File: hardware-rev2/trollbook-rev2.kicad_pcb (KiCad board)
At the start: 4 copper layers, 100 x 100 mm, 150 parts, among them CON1 FPGA JTAG, CON2 CPU JTAG, P1 /BR, P2 /CDIS, P3 Audio, P4 ER-CON40HT-1, P5 Power, P6 Peripheral, P7 VGA, P8 Clocks, P9 Ext. Interrupt, Q1 2N7002E, Q2 2N7002E, Q3 DMP3030SN-7, Q4 2N7002E, Q5 2N7002E, U1 MC68040FC33V, U10 ADA4851-4, U11 33 MHz, U12 12.288 MHz, U2 EPF10K50VRC240, U3 EPC2, U4 HY57V561620, U5 HY57V561620, U6 AS7C34098, U7 74LVC138, U8 MCP4902, U9 S25FL204K0TMFI010

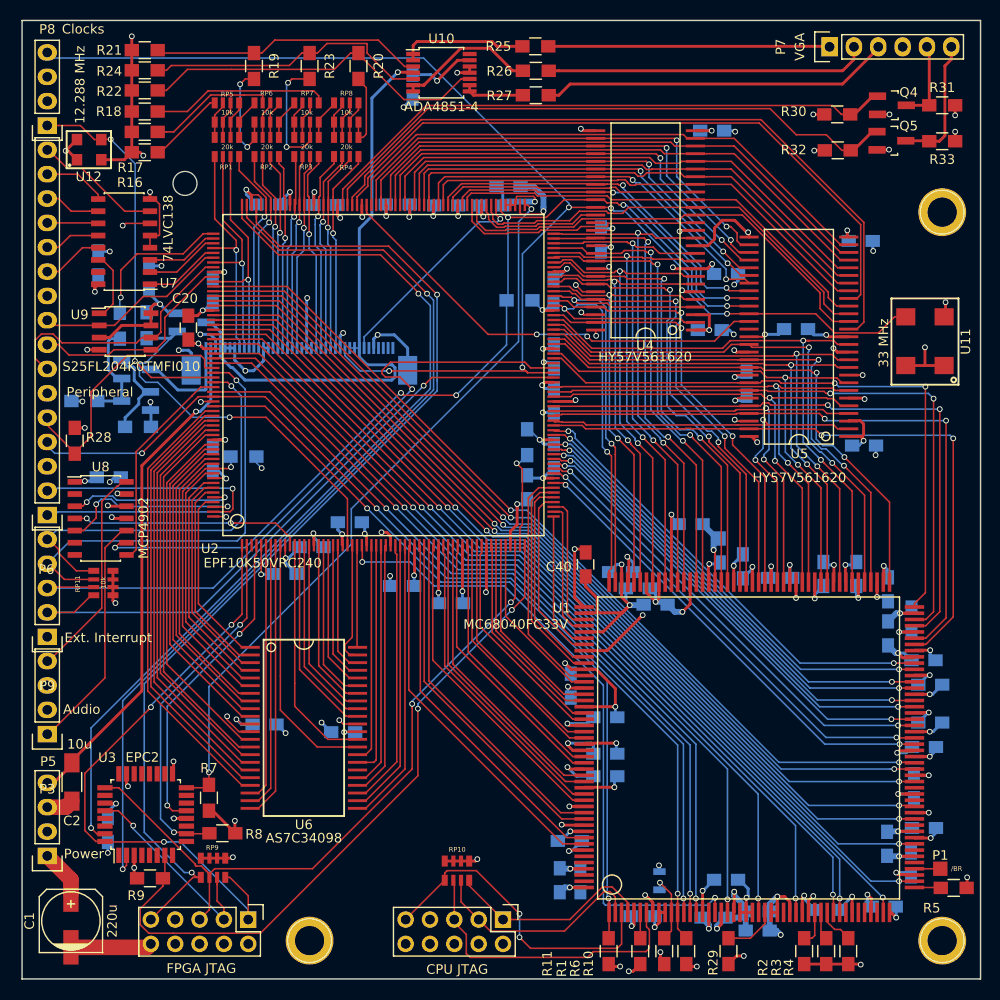
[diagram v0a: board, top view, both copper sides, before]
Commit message: added pcb logo
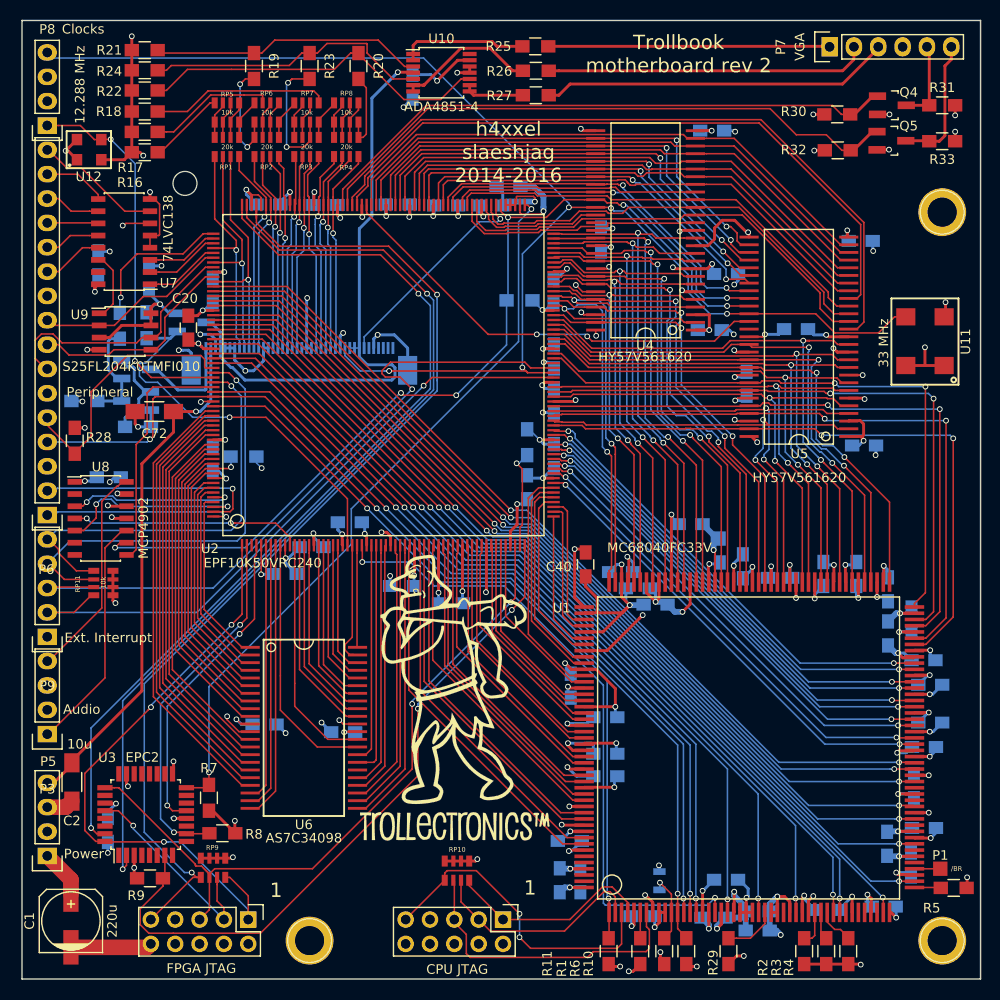
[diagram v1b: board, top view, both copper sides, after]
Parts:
- added C72: 1u, Capacitors_SMD:C_1206_HandSoldering, F.Cu at (98.8, 90.8)
- added G***: LOGO, mod:trollectronics-logo, F.Cu at (130.0, 120.8)
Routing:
- net /SNDSYNC: track 22.3 -> 25.2 mm
- net GND: track 413.5 -> 415.3 mm
- net /VGALED_ANODE: track 53.1 -> 54.5 mm
- net /CPURSTI: track 104.5 -> 105.6 mm
- net /LLA2: track 21.3 -> 20.6 mm
- net /LLD0: track 29.6 -> 29.0 mm
- net /LLD5: track 39.6 -> 38.9 mm
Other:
- board text added: "1"
- board text added: "Trollbook motherboard rev 2"
- board text added: "h4xxel slaeshjag 2014-2016"

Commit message: corrected solder mask minimum width, now there is solder stop everywhere
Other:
- rule solder_mask_min_width: 0.1016 -> 0.0762
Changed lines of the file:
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@@
 (kicad_pcb (version 4) (host pcbnew 0.201602281447+6595~42~ubuntu14.04.1-product)
   (general
-    (links 0)
+    (links 816)
     (no_connects 0)
-    (area 84.924999 49.924999 185.075001 150.075001)
+    (area 52.000001 38.468802 224.934721 153.800001)
     (thickness 1.6)
     (drawings 10)
@@
     (pad_drill 3.048)
     (pad_to_mask_clearance 0.0508)
-    (solder_mask_min_width 0.1016)
+    (solder_mask_min_width 0.0762)
     (aux_axis_origin 0 0)
     (visible_elements FFFFEF7F)
     (pcbplotparams
-      (layerselection 0x01030_ffffffff)
-      (usegerberextensions false)
+      (layerselection 0x010f0_ffffffff)
+      (usegerberextensions true)
       (excludeedgelayer true)
       (linewidth 0.100000)
@@
     (descr "Through hole pin header")
     (tags "pin header")
-    (fp_text reference P3 (at 0 -5.73 180) (layer F.SilkS)
+    (fp_text reference P3 (at 0 -5.73 180) (layer F.SilkS) hide
       (effects (font (size 1 1) (thickness 0.15)))
     )
@@
     (descr "Through hole pin header")
     (tags "pin header")
-    (fp_text reference P5 (at -0.1 9.85 180) (layer F.SilkS)
+    (fp_text reference P5 (at -0.1 9.85 180) (layer F.SilkS) hide
       (effects (font (size 1 1) (thickness 0.15)))
     )
@@
     (descr "Through hole pin header")
     (tags "pin header")
-    (fp_text reference P6 (at 0.1 -5.68 180) (layer F.SilkS)
+    (fp_text reference P6 (at 0.1 -5.68 180) (layer F.SilkS) hide
       (effects (font (size 1 1) (thickness 0.15)))
     )
@@
     (descr "Through hole pin header")
     (tags "pin header")
-    (fp_text reference P7 (at 0 -5.1 90) (layer F.SilkS)
+    (fp_text reference P7 (at 0 -5.1 90) (layer F.SilkS) hide
       (effects (font (size 1 1) (thickness 0.15)))
     )
-    (fp_text value VGA (at 0 -3.1 90) (layer F.SilkS)
+    (fp_text value VGA (at 0.75 -3.5 180) (layer F.SilkS)
       (effects (font (size 1 1) (thickness 0.15)))
     )
@@
     (descr "Through hole pin header")
     (tags "pin header")
-    (fp_text reference P8 (at 0 10.04 180) (layer F.SilkS)
+    (fp_text reference P8 (at 0 10.04 180) (layer F.SilkS) hide
       (effects (font (size 1 1) (thickness 0.15)))
     )
-    (fp_text value Clocks (at -3.745 10.06 180) (layer F.SilkS)
+    (fp_text value Clocks (at -0.12 10.06 180) (layer F.SilkS)
       (effects (font (size 1 1) (thickness 0.15)))
     )
@@
     (descr "Through hole pin header")
     (tags "pin header")
-    (fp_text reference P9 (at 0 -5.1 180) (layer F.SilkS)
+    (fp_text reference P9 (at 0 -5.1 180) (layer F.SilkS) hide
       (effects (font (size 1 1) (thickness 0.15)))
     )

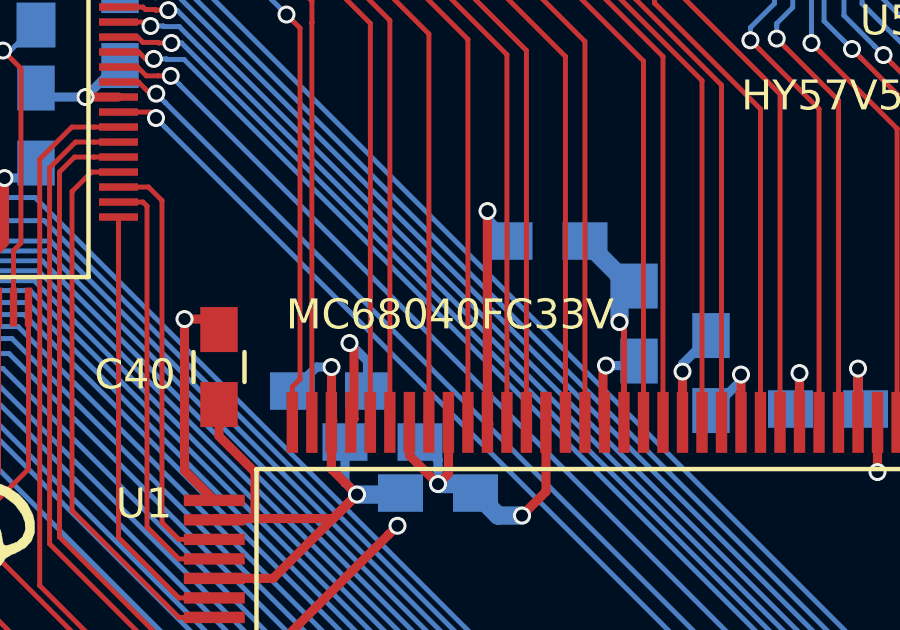
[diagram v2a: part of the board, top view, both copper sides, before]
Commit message: correct cpu name on silk screen
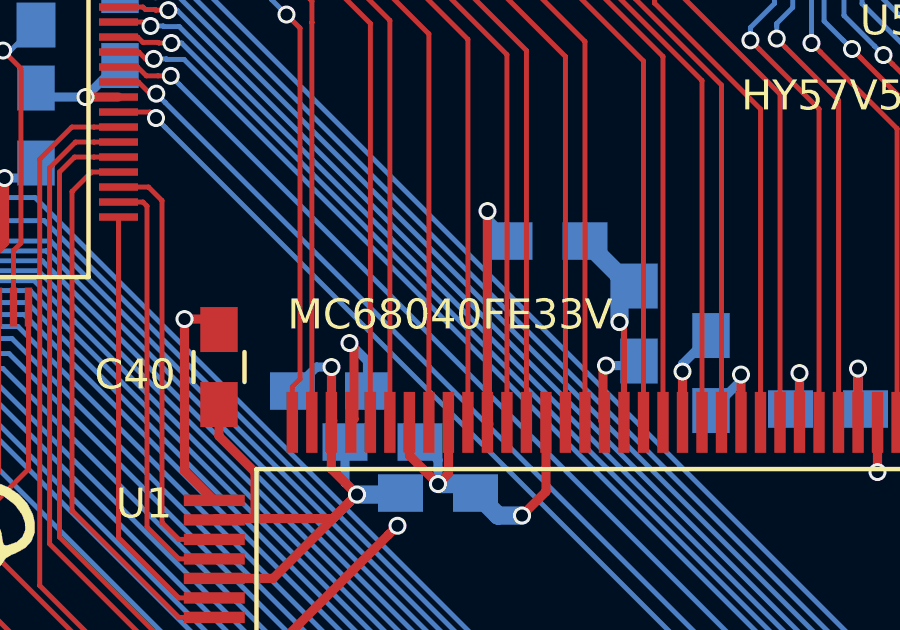
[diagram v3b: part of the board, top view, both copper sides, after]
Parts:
- U1: value MC68040FC33V -> MC68040FE33V
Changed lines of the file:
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@@
     (links 816)
     (no_connects 0)
-    (area 52.000001 38.468802 224.934721 153.800001)
+    (area 84.924999 49.924999 185.075001 150.075001)
     (thickness 1.6)
     (drawings 10)
@@
       (effects (font (size 1 1) (thickness 0.15)))
     )
-    (fp_text value MC68040FC33V (at -9.05 -21.15) (layer F.SilkS)
+    (fp_text value MC68040FE33V (at -9.05 -21.15) (layer F.SilkS)
       (effects (font (size 1 1) (thickness 0.15)))
     )
